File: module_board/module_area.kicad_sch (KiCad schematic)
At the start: 0 parts

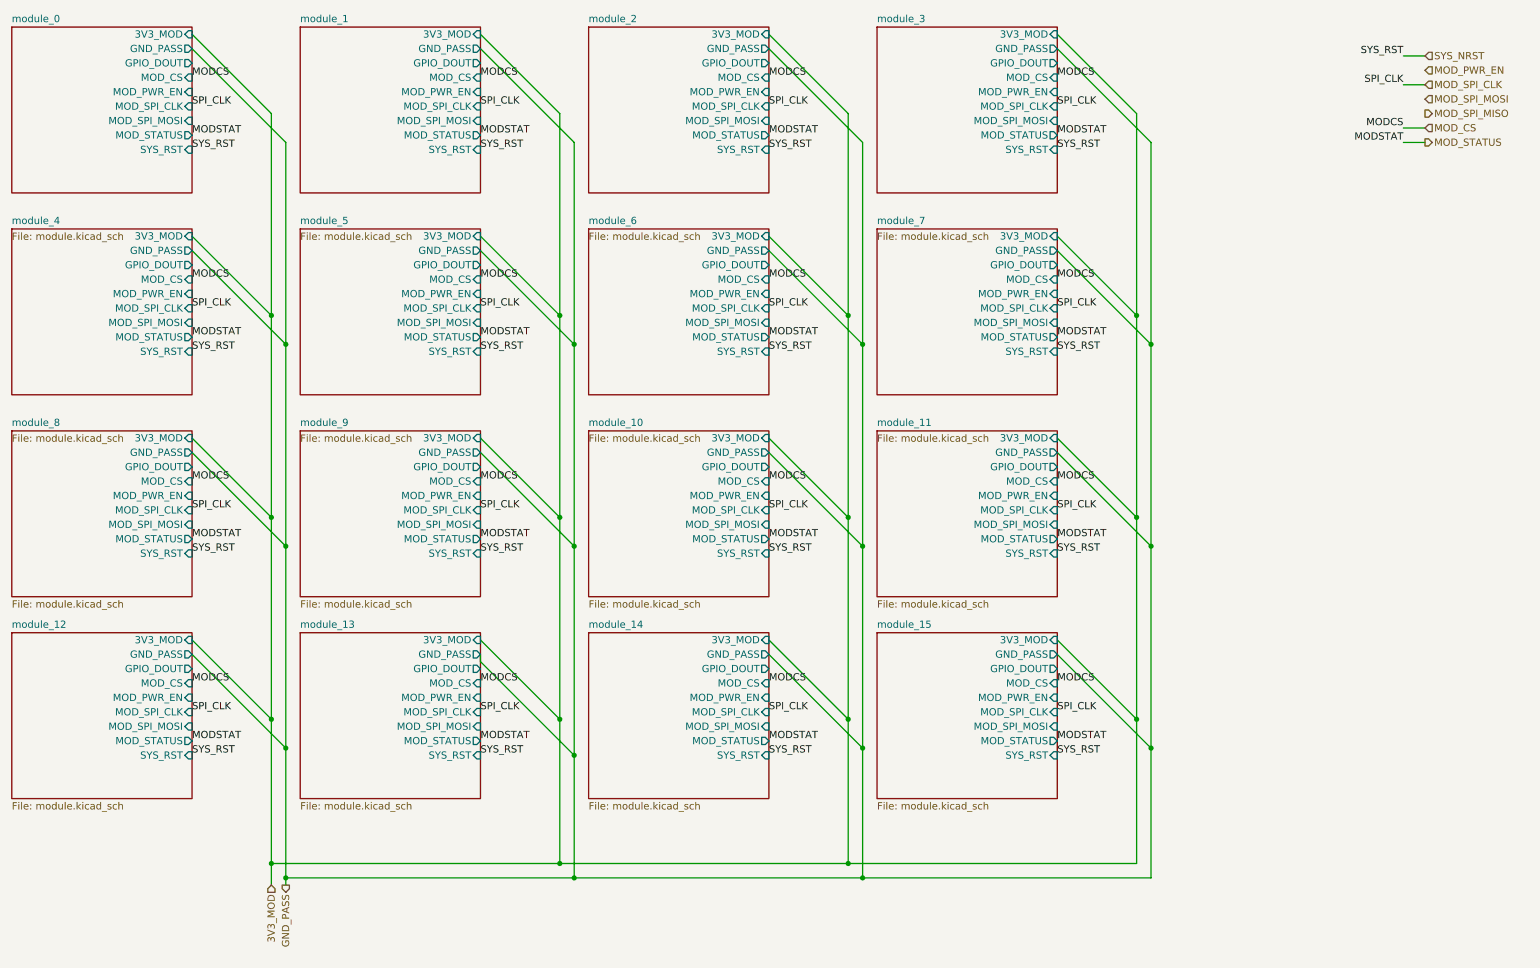
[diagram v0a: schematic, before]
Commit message: feat: finish all essential schematics (i think?)
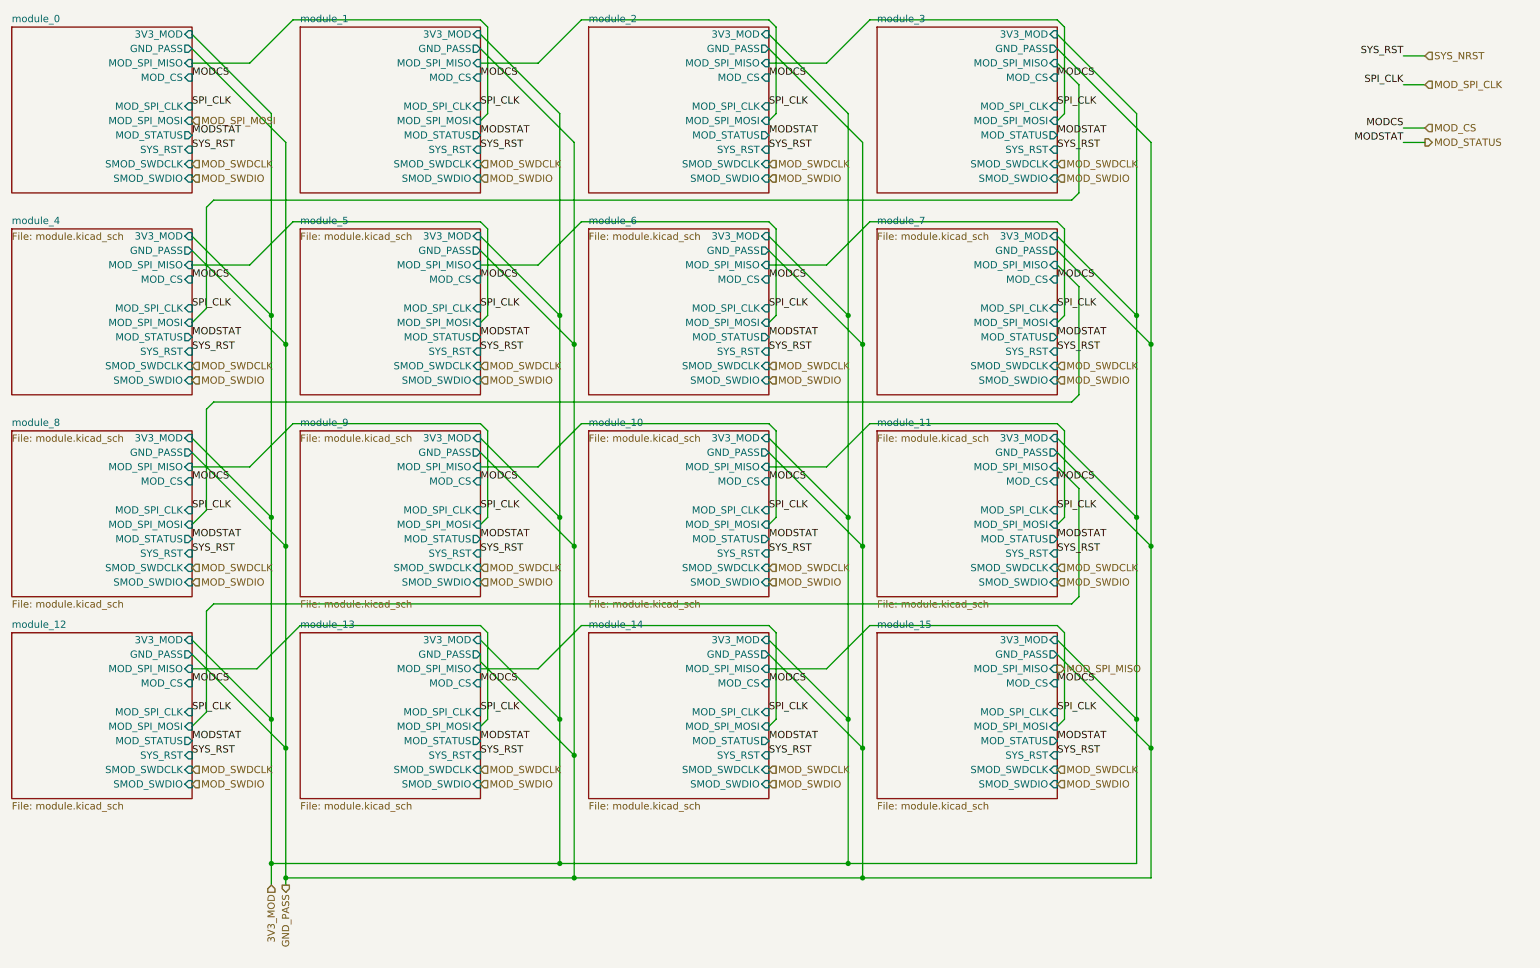
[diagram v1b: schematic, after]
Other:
- sheet module_0 ports: added MOD_SPI_MISO, SMOD_SWDCLK, SMOD_SWDIO; removed GPIO_DOUT, MOD_PWR_EN
- sheet module_1 ports: added MOD_SPI_MISO, SMOD_SWDCLK, SMOD_SWDIO; removed GPIO_DOUT, MOD_PWR_EN
- sheet module_10 ports: added MOD_SPI_MISO, SMOD_SWDCLK, SMOD_SWDIO; removed GPIO_DOUT, MOD_PWR_EN
- sheet module_11 ports: added MOD_SPI_MISO, SMOD_SWDCLK, SMOD_SWDIO; removed GPIO_DOUT, MOD_PWR_EN
- sheet module_12 ports: added MOD_SPI_MISO, SMOD_SWDCLK, SMOD_SWDIO; removed GPIO_DOUT, MOD_PWR_EN
- sheet module_13 ports: added MOD_SPI_MISO, SMOD_SWDCLK, SMOD_SWDIO; removed GPIO_DOUT, MOD_PWR_EN
- sheet module_14 ports: added MOD_SPI_MISO, SMOD_SWDCLK, SMOD_SWDIO; removed GPIO_DOUT, MOD_PWR_EN
- sheet module_15 ports: added MOD_SPI_MISO, SMOD_SWDCLK, SMOD_SWDIO; removed GPIO_DOUT, MOD_PWR_EN
- sheet module_2 ports: added MOD_SPI_MISO, SMOD_SWDCLK, SMOD_SWDIO; removed GPIO_DOUT, MOD_PWR_EN
- sheet module_3 ports: added MOD_SPI_MISO, SMOD_SWDCLK, SMOD_SWDIO; removed GPIO_DOUT, MOD_PWR_EN
- sheet module_4 ports: added MOD_SPI_MISO, SMOD_SWDCLK, SMOD_SWDIO; removed GPIO_DOUT, MOD_PWR_EN
- sheet module_5 ports: added MOD_SPI_MISO, SMOD_SWDCLK, SMOD_SWDIO; removed GPIO_DOUT, MOD_PWR_EN
- sheet module_6 ports: added MOD_SPI_MISO, SMOD_SWDCLK, SMOD_SWDIO; removed GPIO_DOUT, MOD_PWR_EN
- sheet module_7 ports: added MOD_SPI_MISO, SMOD_SWDCLK, SMOD_SWDIO; removed GPIO_DOUT, MOD_PWR_EN
- sheet module_8 ports: added MOD_SPI_MISO, SMOD_SWDCLK, SMOD_SWDIO; removed GPIO_DOUT, MOD_PWR_EN
- sheet module_9 ports: added MOD_SPI_MISO, SMOD_SWDCLK, SMOD_SWDIO; removed GPIO_DOUT, MOD_PWR_EN
